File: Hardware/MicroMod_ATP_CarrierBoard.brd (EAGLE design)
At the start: 86.4 x 55.9 mm, 206 parts, among them J19 QWIIC_RIGHT_ANGLE, J2 JTAG, J20 QWIIC_RIGHT_ANGLE, J21 1X04_SMD_STRAIGHT_COMBO, J4 USB_A_SMT_FEMALE, J6 MICROMOD-2222-C, J8 1X04_SMD_STRAIGHT_COMBO, U5 AP7361C-33

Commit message: Renames LED jumpers to their function
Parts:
- renumbered JP1 to 3V3_LED, JP2 to VIN_LED
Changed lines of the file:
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@@
 <layer number="19" name="Unrouted" color="6" fill="1" visible="yes" active="yes"/>
 <layer number="20" name="Dimension" color="15" fill="1" visible="yes" active="yes"/>
-<layer number="21" name="tPlace" color="16" fill="1" visible="no" active="yes"/>
-<layer number="22" name="bPlace" color="14" fill="1" visible="no" active="yes"/>
+<layer number="21" name="tPlace" color="16" fill="1" visible="yes" active="yes"/>
+<layer number="22" name="bPlace" color="14" fill="1" visible="yes" active="yes"/>
 <layer number="23" name="tOrigins" color="15" fill="1" visible="yes" active="yes"/>
 <layer number="24" name="bOrigins" color="15" fill="1" visible="yes" active="yes"/>
@@
 <layer number="37" name="tTest" color="7" fill="1" visible="no" active="yes"/>
 <layer number="38" name="bTest" color="7" fill="1" visible="no" active="yes"/>
-<layer number="39" name="tKeepout" color="4" fill="11" visible="yes" active="yes"/>
+<layer number="39" name="tKeepout" color="4" fill="11" visible="no" active="yes"/>
 <layer number="40" name="bKeepout" color="1" fill="11" visible="no" active="yes"/>
 <layer number="41" name="tRestrict" color="4" fill="10" visible="no" active="yes"/>
@@
 <attribute name="VALUE" x="3.048" y="8.636" size="0.6096" layer="27" font="vector" ratio="20" rot="R180" align="top-center"/>
 </element>
-<element name="JP1" library="SparkFun-Jumpers" package="SMT-JUMPER_2_NC_TRACE_SILK" package3d_urn="urn:adsk.eagle:package:39281/1" value="JUMPER-SMT_2_NC_TRACE_SILK" x="6.604" y="10.16" smashed="yes" rot="MR0">
+<element name="3V3_LED" library="SparkFun-Jumpers" package="SMT-JUMPER_2_NC_TRACE_SILK" package3d_urn="urn:adsk.eagle:package:39281/1" value="JUMPER-SMT_2_NC_TRACE_SILK" x="6.604" y="10.16" smashed="yes" rot="MR0">
 <attribute name="NAME" x="6.604" y="11.303" size="0.6096" layer="26" font="vector" ratio="20" rot="MR0" align="bottom-center"/>
 <attribute name="VALUE" x="6.604" y="9.017" size="0.6096" layer="28" font="vector" ratio="20" rot="MR0" align="top-center"/>
 </element>
-<element name="JP2" library="SparkFun-Jumpers" package="SMT-JUMPER_2_NC_TRACE_SILK" package3d_urn="urn:adsk.eagle:package:39281/1" value="JUMPER-SMT_2_NC_TRACE_SILK" x="6.604" y="8.128" smashed="yes" rot="MR0">
+<element name="VIN_LED" library="SparkFun-Jumpers" package="SMT-JUMPER_2_NC_TRACE_SILK" package3d_urn="urn:adsk.eagle:package:39281/1" value="JUMPER-SMT_2_NC_TRACE_SILK" x="6.604" y="8.128" smashed="yes" rot="MR0">
 <attribute name="NAME" x="6.604" y="9.271" size="0.6096" layer="26" font="vector" ratio="20" rot="MR0" align="bottom-center"/>
 <attribute name="VALUE" x="6.604" y="6.985" size="0.6096" layer="28" font="vector" ratio="20" rot="MR0" align="top-center"/>
@@
 <contactref element="J9" pad="4"/>
 <contactref element="J11" pad="4"/>
-<contactref element="JP2" pad="2"/>
-<contactref element="JP1" pad="2"/>
+<contactref element="VIN_LED" pad="2"/>
+<contactref element="3V3_LED" pad="2"/>
 <via x="40.1574" y="27.4066" extent="1-16" drill="0.3048"/>
 <via x="31.6484" y="29.591" extent="1-16" drill="0.3048"/>
@@
 <signal name="N$3">
 <contactref element="D2" pad="C"/>
-<contactref element="JP1" pad="1"/>
+<contactref element="3V3_LED" pad="1"/>
 <wire x1="7.481" y1="10.16" x2="8.636" y2="10.16" width="0.1778" layer="1"/>
 <via x="8.636" y="10.16" extent="1-16" drill="0.3048"/>
@@
 <signal name="N$4">
 <contactref element="D3" pad="C"/>
-<contactref element="JP2" pad="1"/>
+<contactref element="VIN_LED" pad="1"/>
 <wire x1="7.481" y1="8.128" x2="8.636" y2="8.128" width="0.1778" layer="1"/>
 <via x="8.636" y="8.128" extent="1-16" drill="0.3048"/>

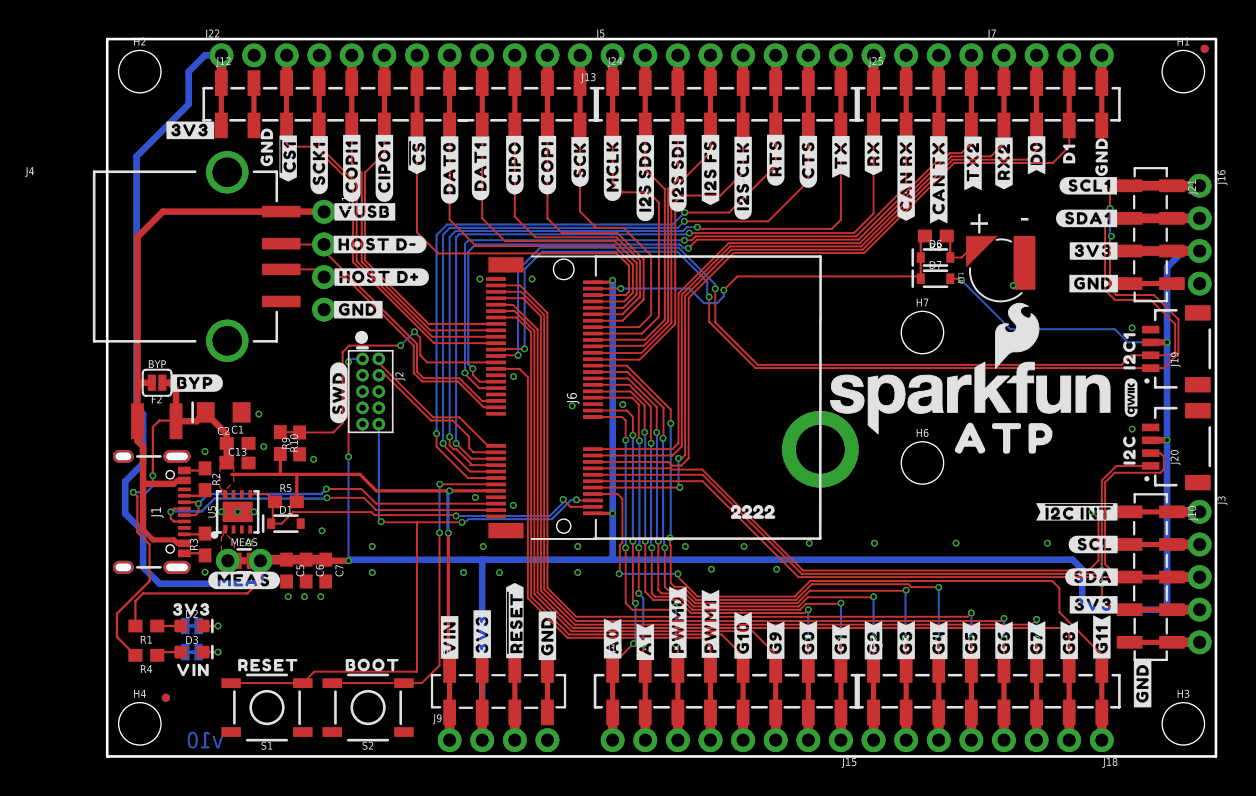
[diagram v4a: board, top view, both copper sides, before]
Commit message: Miters the corners of the board
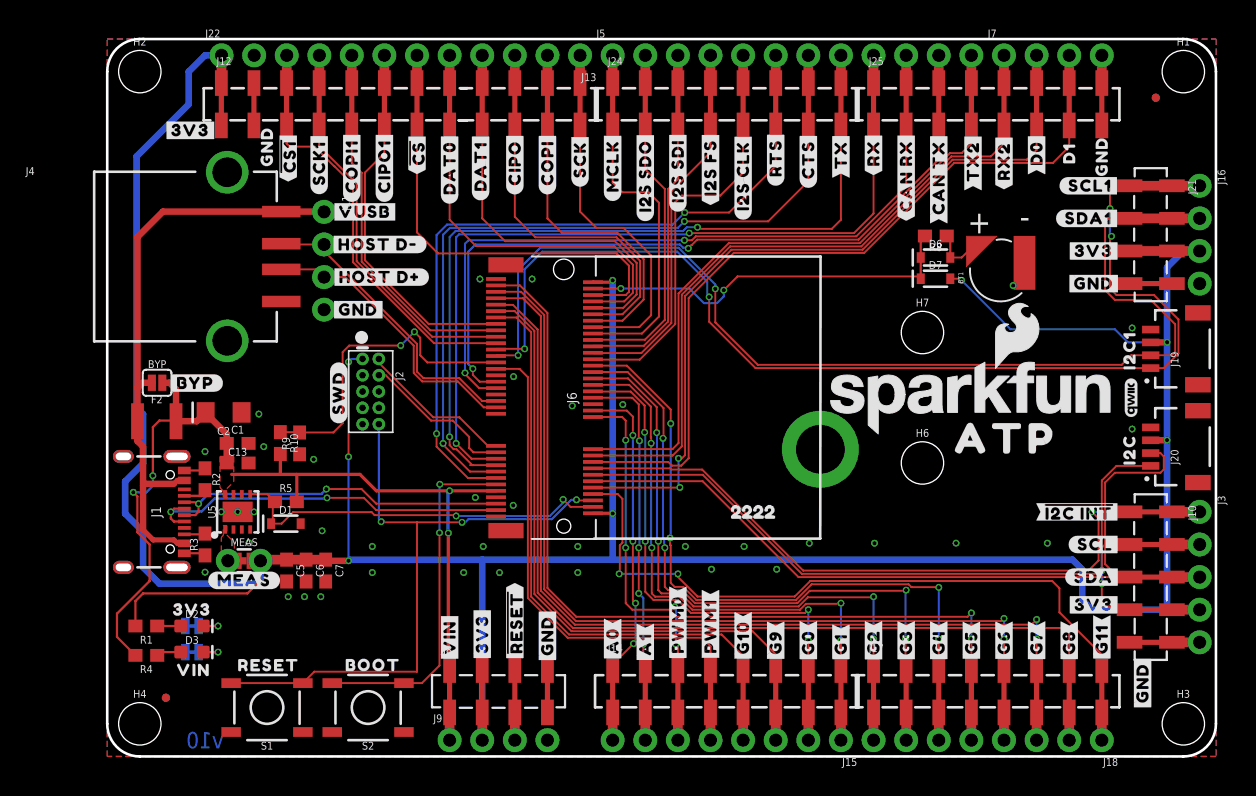
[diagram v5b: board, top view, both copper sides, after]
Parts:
- moved FD2 5.39 mm to (81.7, 51.3)
- moved FD4 5.39 mm to (81.7, 51.3)
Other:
- outline, holes or cut-outs redrawn
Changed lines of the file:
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@@
 <text x="47.498" y="-16.002" size="1.778" layer="51" font="vector" ratio="15">Elias Santistevan</text>
 <dimension x1="0" y1="55.88" x2="0" y2="0" x3="-8.35" y3="27.94" textsize="1.778" layer="47" unit="inch"/>
-<wire x1="0" y1="55.88" x2="86.36" y2="55.88" width="0.2032" layer="20"/>
-<wire x1="86.36" y1="55.88" x2="86.36" y2="0" width="0.2032" layer="20"/>
-<wire x1="86.36" y1="0" x2="0" y2="0" width="0.2032" layer="20"/>
+<wire x1="2.54" y1="55.88" x2="83.82" y2="55.88" width="0.2032" layer="20"/>
+<wire x1="83.82" y1="55.88" x2="86.36" y2="53.34" width="0.2032" layer="20" curve="-90"/>
+<wire x1="86.36" y1="53.34" x2="86.36" y2="2.54" width="0.2032" layer="20"/>
+<wire x1="86.36" y1="2.54" x2="83.82" y2="0" width="0.2032" layer="20" curve="-90"/>
+<wire x1="83.82" y1="0" x2="2.54" y2="0" width="0.2032" layer="20"/>
+<wire x1="2.54" y1="0" x2="0" y2="2.54" width="0.2032" layer="20" curve="-90"/>
+<wire x1="0" y1="2.54" x2="0" y2="53.34" width="0.2032" layer="20"/>
+<wire x1="0" y1="53.34" x2="2.54" y2="55.88" width="0.2032" layer="20" curve="-90"/>
 <dimension x1="83.836" y1="0" x2="0" y2="0" x3="41.918" y3="-5.08" textsize="1.778" layer="47" dtype="horizontal" unit="inch"/>
-<wire x1="0" y1="0" x2="0" y2="55.88" width="0.2032" layer="20"/>
 <circle x="19.812" y="32.639" radius="0.508" width="0" layer="21"/>
 </plain>
@@
 </element>
 <element name="FD1" library="SparkFun-Aesthetics" package="FIDUCIAL-MICRO" value="FIDUCIALUFIDUCIAL" x="4.572" y="4.572" smashed="yes"/>
-<element name="FD2" library="SparkFun-Aesthetics" package="FIDUCIAL-MICRO" value="FIDUCIALUFIDUCIAL" x="85.487" y="55.118" smashed="yes"/>
+<element name="FD2" library="SparkFun-Aesthetics" package="FIDUCIAL-MICRO" value="FIDUCIALUFIDUCIAL" x="81.677" y="51.308" smashed="yes"/>
 <element name="FD3" library="SparkFun-Aesthetics" package="FIDUCIAL-MICRO" value="FIDUCIALUFIDUCIAL" x="4.572" y="4.572" smashed="yes" rot="MR0"/>
-<element name="FD4" library="SparkFun-Aesthetics" package="FIDUCIAL-MICRO" value="FIDUCIALUFIDUCIAL" x="85.487" y="55.118" smashed="yes" rot="MR0"/>
+<element name="FD4" library="SparkFun-Aesthetics" package="FIDUCIAL-MICRO" value="FIDUCIALUFIDUCIAL" x="81.677" y="51.308" smashed="yes" rot="MR0"/>
 <element name="H1" library="SparkFun-Hardware" package="STAND-OFF" value="STAND-OFF" x="83.82" y="53.34" smashed="yes">
 <attribute name="NAME" x="83.82" y="55.372" size="0.6096" layer="25" font="vector" ratio="20" align="bottom-center"/>

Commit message: Swaps qwiic connectors and their respective headers
* Moves headers on teh top and bottom so that they can be placed properly
* Moves the USB host and USB-C connector down so that labels on teh top can fit
* adjusts the traces accordingly to the part movement
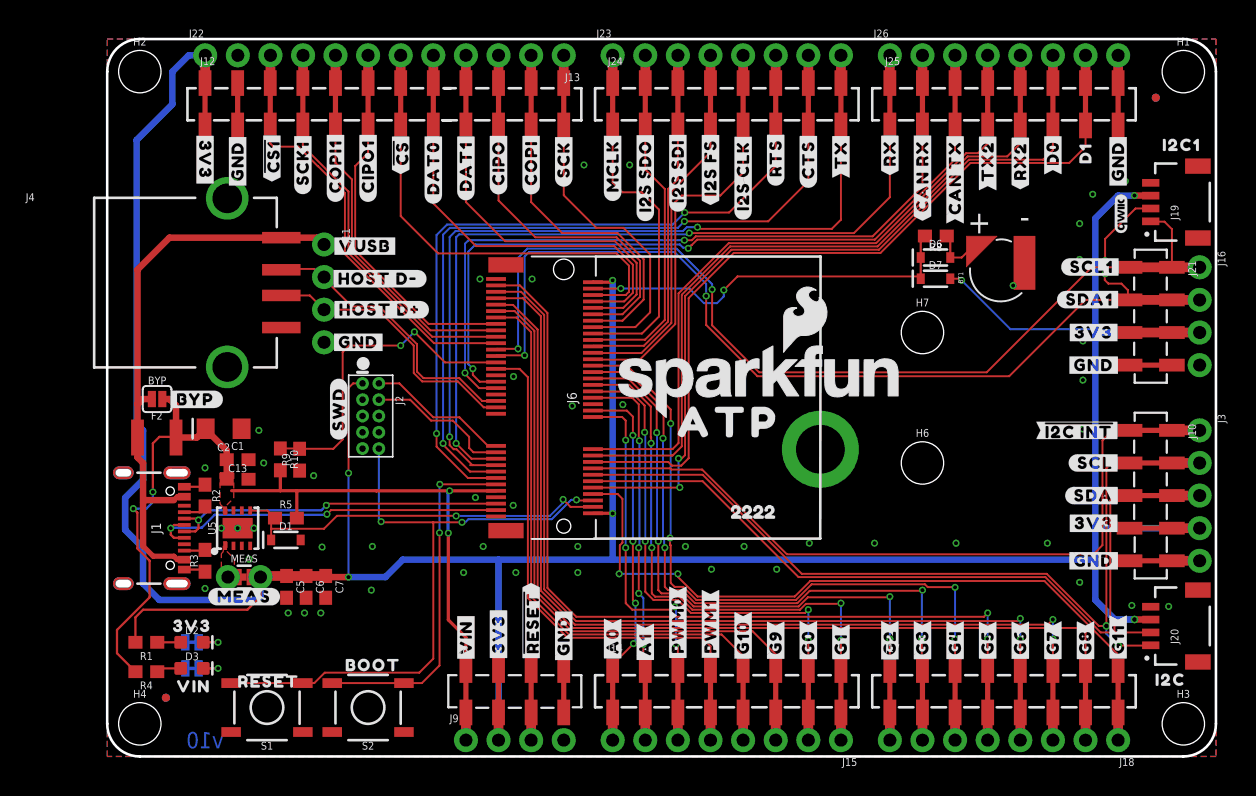
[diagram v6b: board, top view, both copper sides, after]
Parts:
- removed J5: (no value), SparkFun-Connectors:1X12_NO_SILK
- removed J7: (no value), SparkFun-Connectors:1X04_NO_SILK
- added J23, J26: (no value), SparkFun-Connectors:1X08_NO_SILK
- U$3, U$89: device headers_dup:GND4 -> power:#GND#0
- moved U$58 40.7 mm to (78.7, 46.4)
- moved U$3 31.5 mm to (76.8, 15.2), turned to 0 degrees
- moved U$62 21.6 mm to (48.4, 26.0)
- moved U$71 18.2 mm to (82.8, 5.97), turned to 0 degrees
- moved LOGO1 16.6 mm to (50.8, 29.2)
- moved U$72 16.5 mm to (83.7, 47.6), turned to 0 degrees
- moved LOGO2 14.3 mm to (79.0, 42.3)
- moved J20 14.0 mm to (81.3, 10.2)
- moved J19 11.4 mm to (81.3, 43.2)
- moved U$73 8.98 mm to (35.4, 22.6)
- moved LOGO4 7.73 mm to (35.4, 33.7)
- moved J16 6.35 mm to (85.1, 38.1)
- moved J21 6.35 mm to (81.3, 38.1)
- moved U$101 6.35 mm to (82.4, 30.4)
- moved U$70 6.35 mm to (76.8, 18.2)
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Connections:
- net CAN_RXI: now also J26.2; no longer J5.10
- net CAN_TXO: now also J26.3; no longer J5.11
- net CTS1: now also J23.7; no longer J5.7
- net D0: now also J26.6; no longer J7.2
- net D1: now also J26.7; no longer J7.3
- net GND: now also J26.8; no longer J7.4
- net I2S_CLK: now also J23.5; no longer J5.5
- net I2S_SDI: now also J23.3; no longer J5.3
- net I2S_SDO: now also J23.2; no longer J5.2
- net I2S_WS: now also J23.4; no longer J5.4
- net MCLK: now also J23.1; no longer J5.1
- net RTS1: now also J23.6; no longer J5.6
- net RX1: now also J26.1; no longer J5.9
- net RX2: now also J26.5; no longer J7.1
- net TX1: now also J23.8; no longer J5.8
- net TX2: now also J26.4; no longer J5.12
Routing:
- net SCL1: track 89.8 -> 76.1 mm, vias 4 -> 2
- net 3.3V: track 265.3 -> 272.3 mm, vias 8 -> 7
- net SDA1: track 87.7 -> 81.7 mm, vias 2 -> 4
- net I2C_!INT: track 51.8 -> 55.2 mm, vias 2 -> 0
- net G7: track 70.8 -> 72.1 mm
- net G6: track 68.7 -> 69.9 mm
- net G3: track 48.5 -> 49.8 mm
- net G2: track 45.4 -> 46.6 mm
- net CAN_TXO: track 56.1 -> 57.4 mm
- net RX2: track 52.3 -> 53.5 mm
- net D1: track 58.4 -> 59.6 mm
- net TX2: track 49.4 -> 50.7 mm
- net G5: track 66.7 -> 68.0 mm
- net D0: track 57.9 -> 59.2 mm
- net CAN_RXI: track 55.9 -> 57.1 mm
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
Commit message: Moves GND and 3V3 label on top of board along topside of PCB
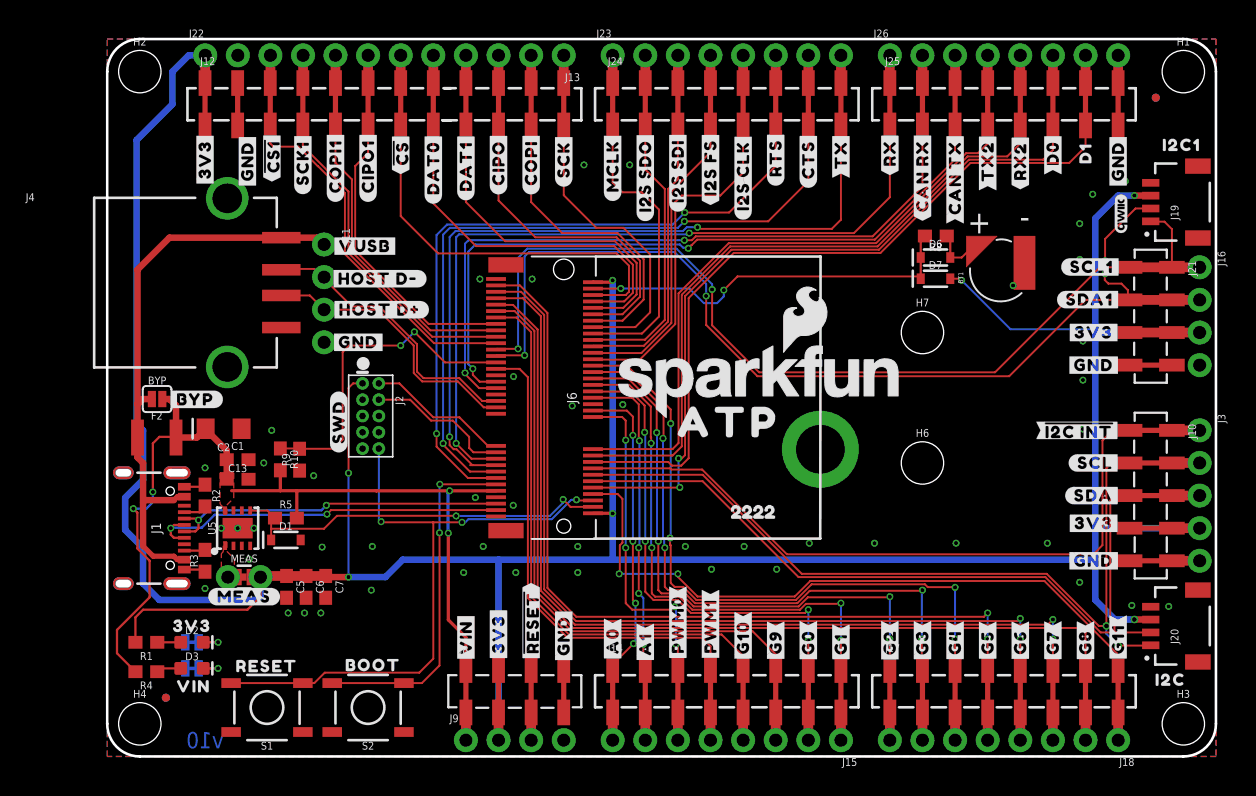
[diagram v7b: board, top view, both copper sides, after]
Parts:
- moved U$5 1.21 mm to (12.4, 7.17)
- moved U$131 1.00 mm to (18.0, 26.1)
- moved U$51 1.00 mm to (18.0, 26.1)
- moved U$89 0.76 mm to (10.9, 46.4)
- turned U$61 to 90 degrees
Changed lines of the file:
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@@
 <setting verticaltext="up"/>
 </settings>
-<grid distance="0.01" unitdist="inch" unit="inch" style="lines" multiple="1" display="yes" altdistance="0.001" altunitdist="inch" altunit="inch"/>
+<grid distance="1" unitdist="mm" unit="mm" style="lines" multiple="1" display="yes" altdistance="0.05" altunitdist="mm" altunit="mm"/>
 <layers>
 <layer number="1" name="Top" color="4" fill="1" visible="yes" active="yes"/>
@@
 <element name="U$40" library="power" package="#HOST_D##9" value="" x="21.209" y="34.798" smashed="yes"/>
 <element name="U$41" library="power" package="#HOST_D##10" value="" x="21.082" y="37.211" smashed="yes"/>
-<element name="U$5" library="power" package="#RESET10" value="" x="12.573" y="5.969" smashed="yes"/>
+<element name="U$5" library="power" package="#RESET10" value="" x="12.423" y="7.169" smashed="yes"/>
 <element name="U$43" library="power" package="BOOT10" value="" x="20.701" y="7.112" smashed="yes"/>
 <element name="U$45" library="power" package="#VIN#6" value="" x="27.94" y="9.271" smashed="yes" rot="R90"/>
@@
 <element name="U$42" library="power" package="#MEAS#10" value="" x="10.668" y="12.446" smashed="yes"/>
 <element name="U$44" library="power" package="#SDA#4" value="" x="76.835" y="20.32" smashed="yes"/>
-<element name="U$51" library="power" package="#SWD#10" value="" x="18.034" y="27.051" smashed="yes" rot="R90"/>
+<element name="U$51" library="power" package="#SWD#10" value="" x="18.034" y="26.051" smashed="yes" rot="R90"/>
 <element name="U$52" library="headtop" package="#I2S_CLK#5" value="" x="49.53" y="45.212" smashed="yes" rot="R90"/>
 <element name="U$53" library="headtop" package="#DAT1#4" value="" x="27.94" y="45.974" smashed="yes" rot="R90"/>
@@
 <element name="U$70" library="power" package="#3V3#1" value="" x="76.835" y="18.161" smashed="yes"/>
 <element name="U$60" library="power" package="#3V3#1" value="" x="76.835" y="33.02" smashed="yes"/>
-<element name="U$61" library="power" package="#3V3#1" value="" x="7.62" y="46.482" smashed="yes" rot="R270"/>
+<element name="U$61" library="power" package="#3V3#1" value="" x="7.62" y="46.482" smashed="yes" rot="R90"/>
 <element name="H6" library="SparkFun-Hardware" package="STAND-OFF" value="STAND-OFF" x="63.5" y="22.86" smashed="yes">
 <attribute name="NAME" x="63.5" y="24.892" size="0.6096" layer="25" font="vector" ratio="20" align="bottom-center"/>
@@
 <element name="U$129" library="fl3" package="#HOST_D##10" value="" x="21.082" y="37.211" smashed="yes" rot="MR0"/>
 <element name="U$130" library="fl3" package="#VUSB#10" value="" x="20.066" y="39.751" smashed="yes" rot="MR0"/>
-<element name="U$131" library="fl3" package="#SWD#10" value="" x="18.034" y="27.051" smashed="yes" rot="MR270"/>
+<element name="U$131" library="fl3" package="#SWD#10" value="" x="18.034" y="26.051" smashed="yes" rot="MR270"/>
 <element name="U$132" library="fl3" package="#MEAS#10" value="" x="10.668" y="12.446" smashed="yes" rot="MR0"/>
 <element name="U$133" library="fl3" package="#VIN_LED#10" value="" x="11.049" y="6.858" smashed="yes" rot="MR0"/>
@@
 <element name="U$3" library="power" package="#GND#0" value="" x="76.835" y="15.24" smashed="yes"/>
 <element name="U$58" library="power" package="#GND#0" value="" x="78.74" y="46.355" smashed="yes" rot="R90"/>
-<element name="U$89" library="power" package="#GND#0" value="" x="10.16" y="46.355" smashed="yes" rot="R90"/>
+<element name="U$89" library="power" package="#GND#0" value="" x="10.922" y="46.355" smashed="yes" rot="R90"/>
 <element name="J23" library="SparkFun-Connectors" package="1X08_NO_SILK" value="" x="39.37" y="54.61" smashed="yes">
 <attribute name="NAME" x="38.1" y="56.007" size="0.6096" layer="25" font="vector" ratio="20"/>
@@
 <via x="16.0782" y="21.8694" extent="1-16" drill="0.3048"/>
 <via x="12.192" y="22.86" extent="1-16" drill="0.3048"/>
-<via x="11.811" y="25.4" extent="1-16" drill="0.3048"/>
+<via x="12.811" y="25.4" extent="1-16" drill="0.3048"/>
 <via x="7.62" y="22.479" extent="1-16" drill="0.3048"/>
 <contactref element="J4" pad="GND"/>
@@
 <wire x1="82.931" y1="41.0718" x2="82.931" y2="38.1" width="0.1524" layer="1"/>
 <wire x1="82.3468" y1="41.656" x2="82.931" y2="41.0718" width="0.1524" layer="1"/>
-<wire x1="50.776" y1="29.9198" x2="68.5024" y2="29.9198" width="0.1524" layer="1"/>
-<wire x1="68.5024" y1="29.9198" x2="76.6826" y2="38.1" width="0.1524" layer="1"/>
-<wire x1="76.6826" y1="38.1" x2="79.375" y2="38.1" width="0.1524" layer="1"/>
+<wire x1="50.776" y1="29.9198" x2="69.1524" y2="29.9198" width="0.1524" layer="1"/>
+<wire x1="69.1524" y1="29.9198" x2="77.3326" y2="38.1" width="0.1524" layer="1"/>
+<wire x1="77.3326" y1="38.1" x2="79.375" y2="38.1" width="0.1524" layer="1"/>
 <wire x1="85.09" y1="38.1" x2="82.93" y2="38.1" width="0" layer="19" extent="1-1"/>
 <wire x1="79.375" y1="38.1" x2="79.63" y2="38.1" width="0" layer="19" extent="1-1"/>
